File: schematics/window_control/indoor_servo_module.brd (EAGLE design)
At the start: 47 x 58.1 mm, 32 parts, among them J1 MTR-SERVO-FS5103B, J2 GND, J3 +5V, J4 OUTDOOR_SIGNAL, J5 J2, J6 J2, J7 J2, Q2 2N3904, Q3 2N3906BU, Q4 2N3904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

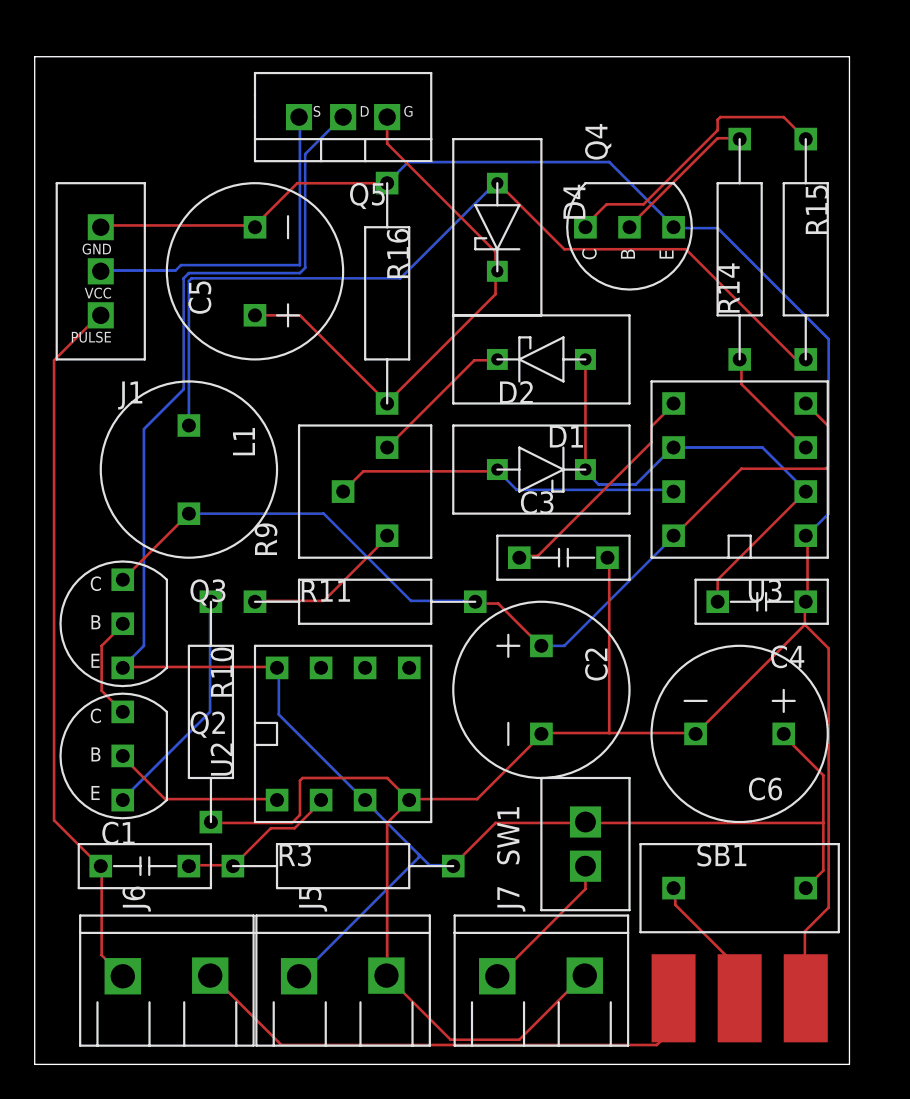
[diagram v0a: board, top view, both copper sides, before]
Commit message: Servo module ready, but i will change connectors
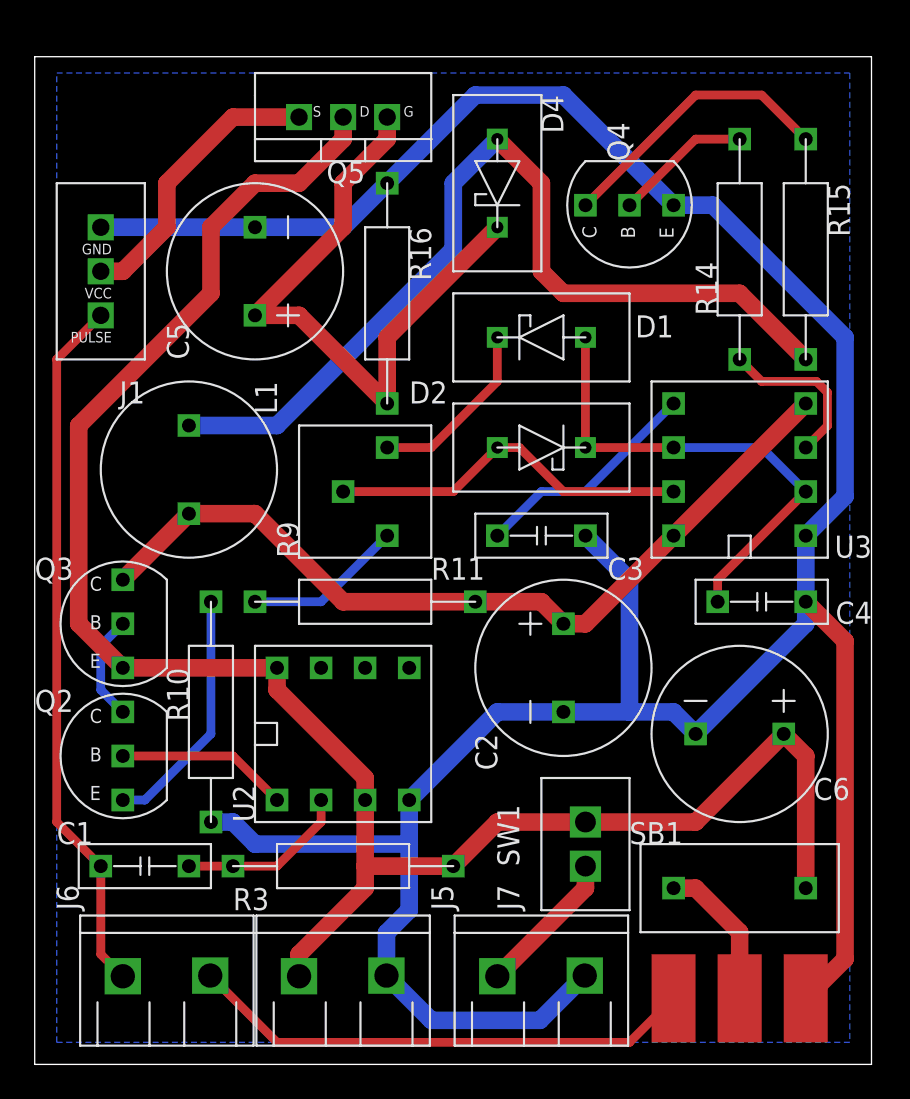
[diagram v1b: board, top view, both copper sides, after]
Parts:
- moved D4 2.54 mm to (63.5, 41.9)
- moved C2 1.80 mm to (67.3, 14.0)
- moved C3 1.80 mm to (66.0, 21.6)
- moved D1 1.27 mm to (66.0, 33.0)
- moved D2 1.27 mm to (66.0, 26.7)
- moved Q4 1.27 mm to (72.4, 39.4)
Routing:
- net N$51: track 31.5 -> 37.1 mm
- net GND: track 164.3 -> 169.6 mm
- net +5V_IF_EN: track 53.9 -> 48.8 mm
- net N$40: track 20.2 -> 16.6 mm
- net N$35: track 6.71 -> 9.54 mm
- net N$39: track 50.5 -> 52.9 mm
- net N$48: track 8.45 -> 10.5 mm
- net N$46: track 29.9 -> 28.6 mm
- net +5V: track 108.8 -> 107.7 mm
- net OUTDOOR_SIGNAL: track 30.5 -> 29.4 mm
- net N$47: track 20.1 -> 21.2 mm
- net N$5: track 7.95 -> 8.74 mm
- net N$38: track 13.5 -> 14.3 mm
- net N$53: track 9.32 -> 9.94 mm
- net N$2: track 8.52 -> 7.93 mm
- added copper zone on layer 16, net GND
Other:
- board size 47 x 58.1 mm -> 48.2 x 58.1 mm

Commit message: Servo module - added holes
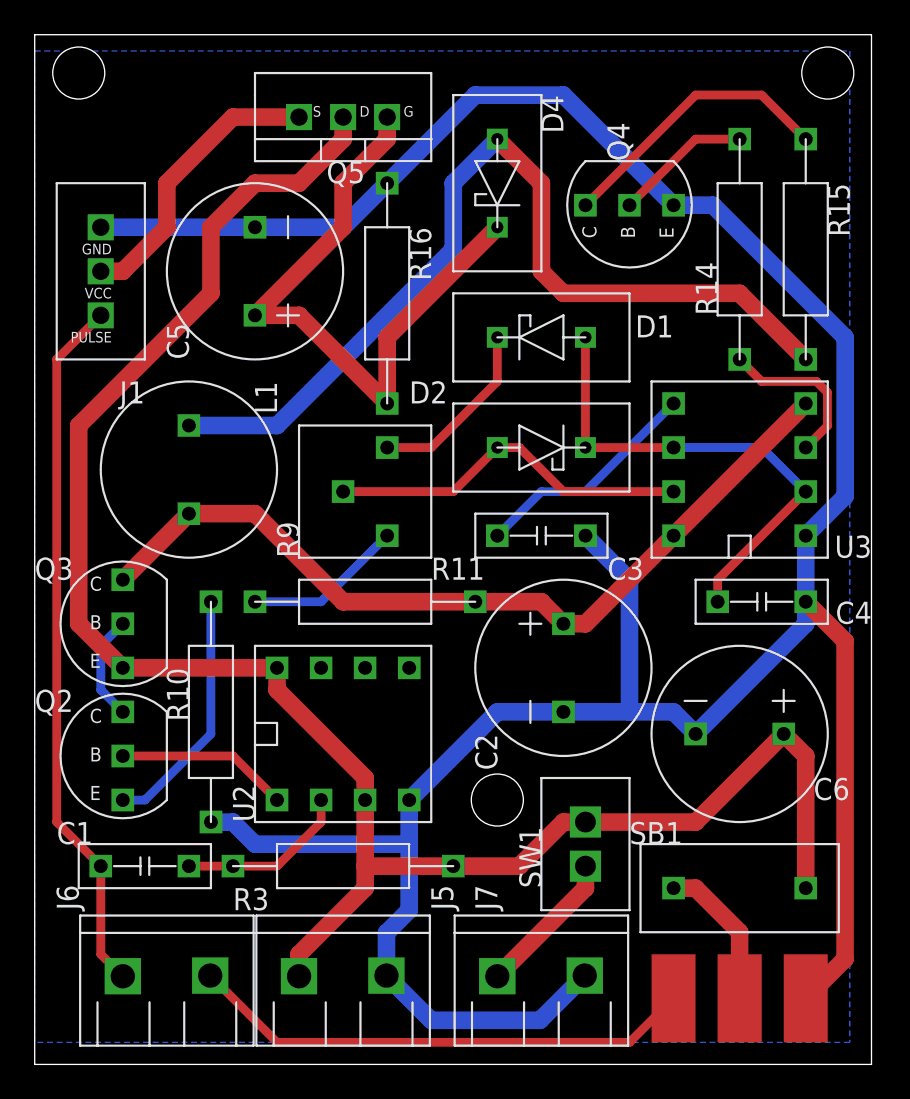
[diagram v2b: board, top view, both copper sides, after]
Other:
- board size 48.2 x 58.1 mm -> 48.2 x 59.4 mm
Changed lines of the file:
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@@
 <drawing>
 <settings>
-<setting alwaysvectorfont="yes"/>
+<setting alwaysvectorfont="no"/>
 <setting verticaltext="up"/>
 </settings>
@@
 <layer number="43" name="vRestrict" color="2" fill="10" visible="yes" active="yes"/>
 <layer number="44" name="Drills" color="7" fill="1" visible="no" active="yes"/>
-<layer number="45" name="Holes" color="7" fill="1" visible="no" active="yes"/>
+<layer number="45" name="Holes" color="7" fill="1" visible="yes" active="yes"/>
 <layer number="46" name="Milling" color="3" fill="1" visible="no" active="yes"/>
 <layer number="47" name="Measures" color="7" fill="1" visible="no" active="yes"/>
@@
 <plain>
 <wire x1="36.83" y1="-8.89" x2="85.07" y2="-8.89" width="0" layer="20"/>
-<wire x1="85.07" y1="-8.89" x2="85.07" y2="49.2" width="0" layer="20"/>
-<wire x1="85.07" y1="49.2" x2="36.83" y2="49.2" width="0" layer="20"/>
-<wire x1="36.83" y1="49.2" x2="36.83" y2="-8.89" width="0" layer="20"/>
+<wire x1="85.07" y1="-8.89" x2="85.07" y2="50.47" width="0" layer="20"/>
+<wire x1="85.07" y1="50.47" x2="36.83" y2="50.47" width="0" layer="20"/>
+<wire x1="36.83" y1="50.47" x2="36.83" y2="-8.89" width="0" layer="20"/>
+<hole x="39.37" y="48.26" drill="3"/>
+<hole x="82.55" y="48.26" drill="3"/>
+<hole x="63.5" y="6.35" drill="3"/>
 </plain>
 <attributes>
@@
 </element>
 <element name="J7" library="my_devices" package="J2" value="J2" x="66.04" y="-3.81" smashed="yes" rot="R90">
-<attribute name="NAME" x="64.77" y="0" size="1.27" layer="21" rot="R90"/>
+<attribute name="NAME" x="63.5" y="0" size="1.27" layer="21" rot="R90"/>
 </element>
 <element name="L1" library="my_devices" package="L-RLB0914" value="RLB0914-102KL, 1000 uH" x="45.72" y="25.4" smashed="yes" rot="R270">
@@
 </element>
 <element name="SW1" library="my_devices" package="SWITCH" value="SWITCH" x="68.58" y="3.81" smashed="yes" rot="R90">
-<attribute name="NAME" x="64.77" y="2.54" size="1.27" layer="21" rot="R90"/>
+<attribute name="NAME" x="66.04" y="1.27" size="1.27" layer="21" rot="R90"/>
 </element>
 <element name="U2" library="my_devices" package="DIP8" value="LM311P" x="54.61" y="10.16" smashed="yes" rot="R90">
@@
 <wire x1="68.58" y1="5.08" x2="74.93" y2="5.08" width="1.016" layer="1"/>
 <wire x1="74.93" y1="5.08" x2="80.01" y2="10.16" width="1.016" layer="1"/>
-<wire x1="63.5" y1="5.08" x2="60.96" y2="2.54" width="1.016" layer="1"/>
-<wire x1="68.58" y1="5.08" x2="63.5" y2="5.08" width="1.016" layer="1"/>
 <wire x1="52.07" y1="-3.81" x2="52.07" y2="-2.54" width="1.016" layer="1"/>
 <wire x1="52.07" y1="-2.54" x2="55.88" y2="1.27" width="1.016" layer="1"/>
@@
 <wire x1="54.61" y1="44.45" x2="54.61" y2="45.72" width="1.016" layer="1"/>
 <wire x1="39.37" y1="27.94" x2="46.99" y2="35.56" width="1.016" layer="1"/>
+<wire x1="60.96" y1="2.54" x2="64.77" y2="2.54" width="1.016" layer="1"/>
+<wire x1="64.77" y1="2.54" x2="67.31" y2="5.08" width="1.016" layer="1"/>
+<wire x1="67.31" y1="5.08" x2="68.58" y2="5.08" width="1.016" layer="1"/>
 </signal>
 <signal name="GND">
@@
 <wire x1="62.23" y1="46.99" x2="67.31" y2="46.99" width="1.016" layer="16"/>
 <wire x1="67.31" y1="46.99" x2="73.66" y2="40.64" width="1.016" layer="16"/>
-<polygon width="0.508" layer="16" isolate="0.4064">
-<vertex x="38.1" y="48.26"/>
-<vertex x="83.82" y="48.26"/>
+<polygon width="0.1524" layer="16">
+<vertex x="36.83" y="49.53"/>
+<vertex x="83.82" y="49.53"/>
 <vertex x="83.82" y="-7.62"/>
-<vertex x="38.1" y="-7.62"/>
+<vertex x="36.83" y="-7.62"/>
 </polygon>
 </signal>
